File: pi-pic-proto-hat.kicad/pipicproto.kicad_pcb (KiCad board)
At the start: 2 copper layers, 65 x 56 mm, 24 parts, among them J1 RUN/~PGM~, J10 Conn_01x13_Male, J22 Conn_01x13_Male, J6 Barrel_Jack_Switch, J7 Conn_01x24_Male, J8 Conn_01x06_Male, J9 Conn_01x02_Male, P1 Conn_02x20_Odd_Even, Q1 IRF4905, U1 PIC12F675-IP

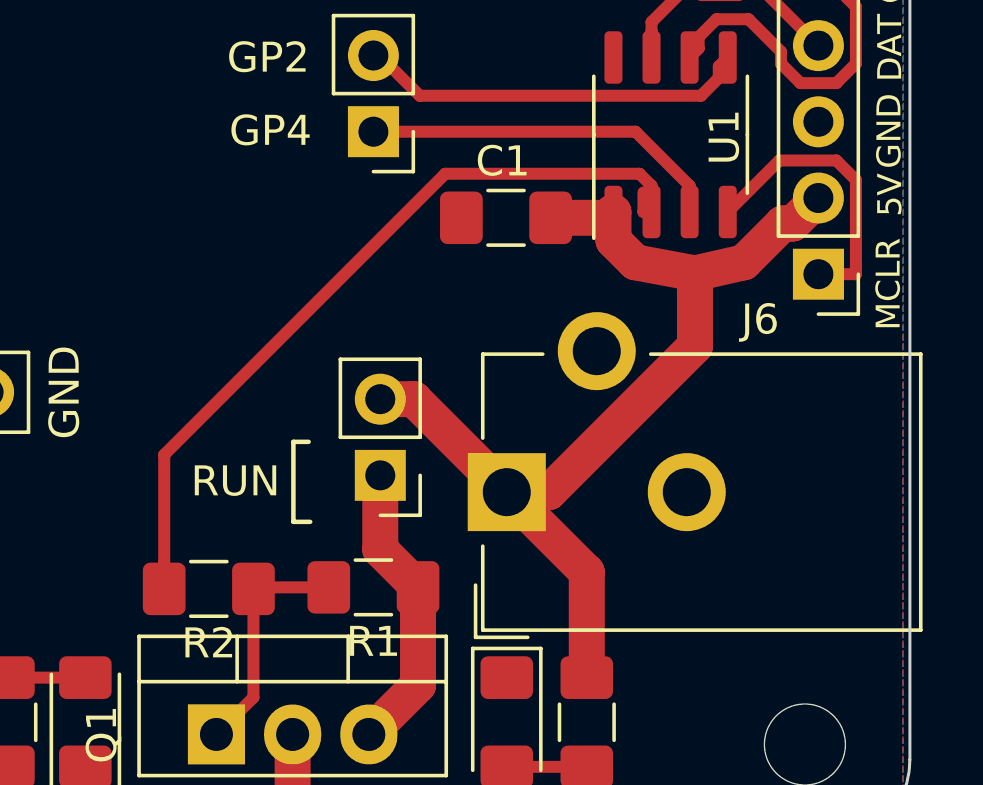
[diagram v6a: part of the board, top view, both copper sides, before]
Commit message: V2.12: changed position of RUN-jumper
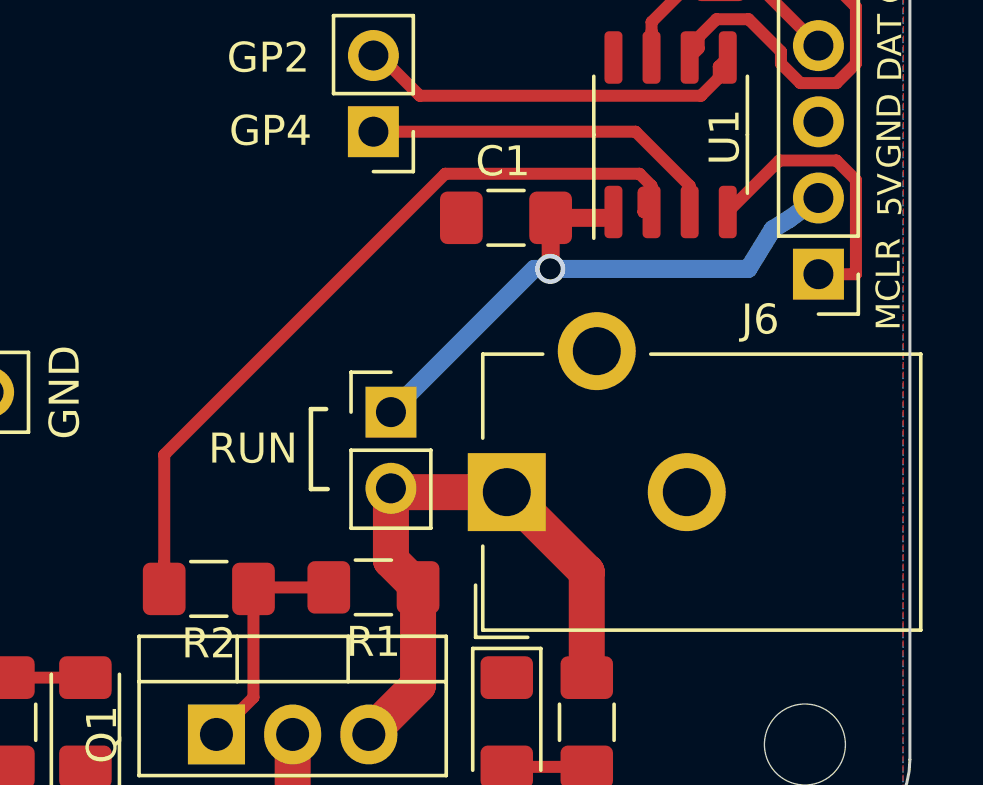
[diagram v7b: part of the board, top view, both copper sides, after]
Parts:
- moved J1 2.14 mm to (247.7, 135.4), turned to 0 degrees
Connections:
- J1 pad 1: +5P -> +5VP
- J1 pad 2: +5VP -> +5P
- J6 pad 1: +5VP -> +5P
- R4 pad 2: +5VP -> +5P
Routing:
- net +5VP: track 34.7 -> 20.9 mm, vias 0 -> 1
- net +5P: track 9.84 -> 20.5 mm
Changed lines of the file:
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@@
     (thickness 1.6)
     (drawings 67)
-    (tracks 227)
+    (tracks 225)
     (zones 0)
     (modules 24)
@@
     (fp_line (start -1.6 0.8) (end -1.6 -0.8) (layer F.Fab) (width 0.1))
     (pad 2 smd roundrect (at 1.4875 0 90) (size 1.425 1.75) (layers F.Cu F.Paste F.Mask) (roundrect_rratio 0.175439)
-      (net 30 +5VP))
+      (net 43 +5P))
     (pad 1 smd roundrect (at -1.4875 0 90) (size 1.425 1.75) (layers F.Cu F.Paste F.Mask) (roundrect_rratio 0.175439)
       (net 45 "Net-(D2-Pad2)"))
@@
   )
   (module Connector_PinHeader_2.54mm:PinHeader_1x02_P2.54mm_Vertical (layer F.Cu)
-    (at 247.3456 137.5286 180)
+    (at 247.7012 135.4204)
     (descr "Through hole straight pin header, 1x02, 2.54mm pitch, single row")
     (tags "Through hole pin header THT 1x02 2.54mm single row")
@@
       (effects (font (size 1 1) (thickness 0.15)))
     )
-    (pad 1 thru_hole rect (at 0 0 180) (size 1.7 1.7) (drill 1) (layers *.Cu *.Mask)
+    (pad 1 thru_hole rect (at 0 0) (size 1.7 1.7) (drill 1) (layers *.Cu *.Mask)
+      (net 30 +5VP))
+    (pad 2 thru_hole oval (at 0 2.54) (size 1.7 1.7) (drill 1) (layers *.Cu *.Mask)
       (net 43 +5P))
-    (pad 2 thru_hole oval (at 0 2.54 180) (size 1.7 1.7) (drill 1) (layers *.Cu *.Mask)
-      (net 30 +5VP))
     (model ${KISYS3DMOD}/Connector_PinHeader_2.54mm.3dshapes/PinHeader_1x02_P2.54mm_Vertical.wrl
       (at (xyz 0 0 0))
@@
     (fp_line (start -4.5 10.2) (end 4.5 10.2) (layer F.Fab) (width 0.1))
     (pad 1 thru_hole rect (at 0 0 90) (size 2.6 2.6) (drill 1.6) (layers *.Cu *.Mask)
-      (net 30 +5VP))
+      (net 43 +5P))
     (pad 2 thru_hole circle (at 0 6 90) (size 2.6 2.6) (drill 1.6) (layers *.Cu *.Mask)
       (net 3 GND))
@@
     (effects (font (size 0.8 0.8) (thickness 0.1)))
   )
-  (gr_line (start 244.45 139.078) (end 245.0088 139.078) (layer F.SilkS) (width 0.15))
-  (gr_line (start 244.45 136.411) (end 244.45 139.078) (layer F.SilkS) (width 0.15))
-  (gr_line (start 244.958 136.411) (end 244.45 136.411) (layer F.SilkS) (width 0.15))
-  (gr_text RUN (at 242.5196 137.7318) (layer F.SilkS)
+  (gr_line (start 245.0342 137.9858) (end 245.593 137.9858) (layer F.SilkS) (width 0.15))
+  (gr_line (start 245.0342 135.3188) (end 245.0342 137.9858) (layer F.SilkS) (width 0.15))
+  (gr_line (start 245.5422 135.3188) (end 245.0342 135.3188) (layer F.SilkS) (width 0.15))
+  (gr_text RUN (at 243.1038 136.6396) (layer F.SilkS)
     (effects (font (size 1 1) (thickness 0.15)))
   )
@@
   (segment (start 250.260001 97.480001) (end 249.01 96.23) (width 0.4) (layer F.Cu) (net 3) (status 20))
   (segment (start 255.340001 97.480001) (end 250.260001 97.480001) (width 0.4) (layer F.Cu) (net 3))
+  (segment (start 250.0491 128.9434) (end 250.0491 129.0593) (width 0.4) (layer F.Cu) (net 3))
   (segment (start 246.99 101.83) (end 246.99 103.01) (width 0.4) (layer F.Cu) (net 6) (status 20))
   (segment (start 243.93 98.77) (end 246.99 101.83) (width 0.4) (layer F.Cu) (net 6) (status 10))
@@
   (segment (start 257.479999 97.079999) (end 257.50208 97.079999) (width 0.4) (layer B.Cu) (net 29))
   (segment (start 256.63 96.23) (end 257.479999 97.079999) (width 0.4) (layer B.Cu) (net 29) (status 10))
-  (segment (start 255.118 129.698318) (end 255.118 128.7498) (width 1.2) (layer F.Cu) (net 30) (status 20))
-  (segment (start 255.844492 130.42481) (end 255.118 129.698318) (width 1.2) (layer F.Cu) (net 30))
-  (segment (start 260.763319 129.132999) (end 259.471508 130.42481) (width 1.2) (layer F.Cu) (net 30))
-  (segment (start 261.100601 129.132999) (end 260.763319 129.132999) (width 1.2) (layer F.Cu) (net 30))
-  (segment (start 261.9506 128.283) (end 261.100601 129.132999) (width 1.2) (layer F.Cu) (net 30) (status 10))
-  (segment (start 254.9101 128.9577) (end 255.118 128.7498) (width 1.2) (layer F.Cu) (net 30) (status 30))
-  (segment (start 254.8958 128.9434) (end 254.9101 128.9577) (width 1.2) (layer F.Cu) (net 30) (status 30))
-  (segment (start 253.0241 128.9434) (end 254.8958 128.9434) (width 1.2) (layer F.Cu) (net 30) (status 30))
-  (segment (start 252.970002 138.0874) (end 257.8358 133.221602) (width 1.2) (layer F.Cu) (net 30))
-  (segment (start 257.8358 133.221602) (end 257.8358 130.7976) (width 1.2) (layer F.Cu) (net 30))
-  (segment (start 251.562 138.0874) (end 252.970002 138.0874) (width 1.2) (layer F.Cu) (net 30) (status 10))
-  (segment (start 259.471508 130.42481) (end 257.8358 130.7976) (width 1.2) (layer F.Cu) (net 30))
-  (segment (start 257.8358 130.7976) (end 255.844492 130.42481) (width 1.2) (layer F.Cu) (net 30))
-  (segment (start 248.4632 134.9886) (end 247.3456 134.9886) (width 1.2) (layer F.Cu) (net 30))
-  (segment (start 251.562 138.0874) (end 248.4632 134.9886) (width 1.2) (layer F.Cu) (net 30))
-  (segment (start 254.229 140.7544) (end 251.562 138.0874) (width 1.2) (layer F.Cu) (net 30))
-  (segment (start 254.229 144.2707) (end 254.229 140.7544) (width 1.2) (layer F.Cu) (net 30))
+  (via (at 253.0098 130.6452) (size 1) (drill 0.7) (layers F.Cu B.Cu) (net 30))
+  (segment (start 253.0241 128.9434) (end 253.0241 130.6309) (width 0.6) (layer F.Cu) (net 30))
+  (segment (start 253.0241 130.6309) (end 253.0098 130.6452) (width 0.6) (layer F.Cu) (net 30))
+  (segment (start 260.96 128.9942) (end 261.9506 128.283) (width 0.6) (layer B.Cu) (net 30))
+  (segment (start 260.4266 129.3244) (end 260.96 128.9942) (width 0.6) (layer B.Cu) (net 30))
+  (segment (start 253.0098 130.6452) (end 259.6138 130.6452) (width 0.6) (layer B.Cu) (net 30))
+  (segment (start 259.6138 130.6452) (end 260.4266 129.3244) (width 0.6) (layer B.Cu) (net 30))
+  (segment (start 252.4764 130.6452) (end 247.7012 135.4204) (width 0.6) (layer B.Cu) (net 30))
+  (segment (start 253.0098 130.6452) (end 252.4764 130.6452) (width 0.6) (layer B.Cu) (net 30))
+  (segment (start 253.0241 128.9434) (end 254.9244 128.9434) (width 0.6) (layer F.Cu) (net 30))
+  (segment (start 254.229 140.7544) (end 251.562 138.0874) (width 1.2) (layer F.Cu) (net 43))
+  (segment (start 254.229 144.2707) (end 254.229 140.7544) (width 1.2) (layer F.Cu) (net 43))
   (segment (start 263.5876 114.6321) (end 264.0842 115.1287) (width 0.4) (layer F.Cu) (net 33))
   (segment (start 262.7126 114.6321) (end 263.5876 114.6321) (width 0.4) (layer F.Cu) (net 33) (status 10))
@@
   (segment (start 257.658 127.8748) (end 255.8564 126.0732) (width 0.4) (layer F.Cu) (net 42) (status 10))
   (segment (start 257.658 128.7498) (end 257.658 127.8748) (width 0.4) (layer F.Cu) (net 42) (status 30))
-  (segment (start 247.3456 140.0035) (end 248.6045 141.2624) (width 1.2) (layer F.Cu) (net 43))
-  (segment (start 247.3456 137.5286) (end 247.3456 140.0035) (width 1.2) (layer F.Cu) (net 43))
   (segment (start 248.6045 144.5247) (end 246.9646 146.1646) (width 1.2) (layer F.Cu) (net 43))
   (segment (start 248.6045 141.2624) (end 248.6045 144.5247) (width 1.2) (layer F.Cu) (net 43))
+  (segment (start 247.8282 138.0874) (end 247.7012 137.9604) (width 1.2) (layer F.Cu) (net 43))
+  (segment (start 251.562 138.0874) (end 247.8282 138.0874) (width 1.2) (layer F.Cu) (net 43))
+  (segment (start 247.7012 140.3591) (end 248.6045 141.2624) (width 1.2) (layer F.Cu) (net 43))
+  (segment (start 247.7012 137.9604) (end 247.7012 140.3591) (width 1.2) (layer F.Cu) (net 43))
   (segment (start 237.5158 144.2707) (end 234.9504 144.2707) (width 0.4) (layer F.Cu) (net 44))
   (segment (start 254.229 147.2457) (end 251.562 147.2457) (width 0.4) (layer F.Cu) (net 45))

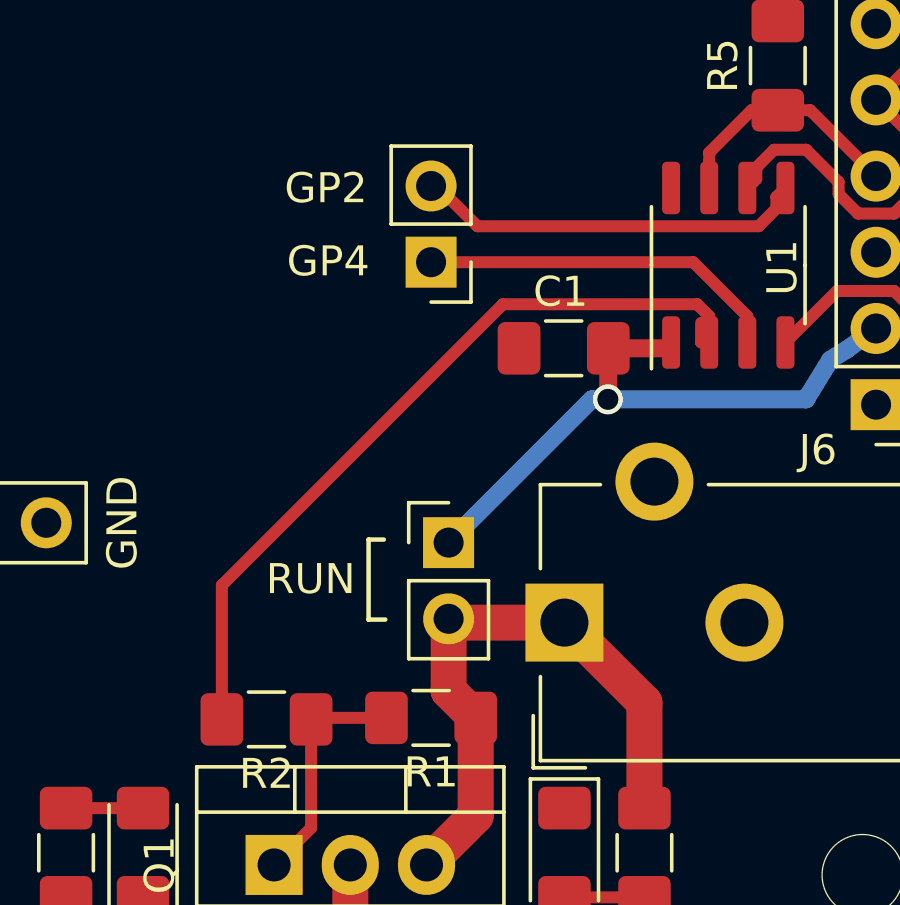
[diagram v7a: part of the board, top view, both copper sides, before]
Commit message: V2.13: added button connected to GP2
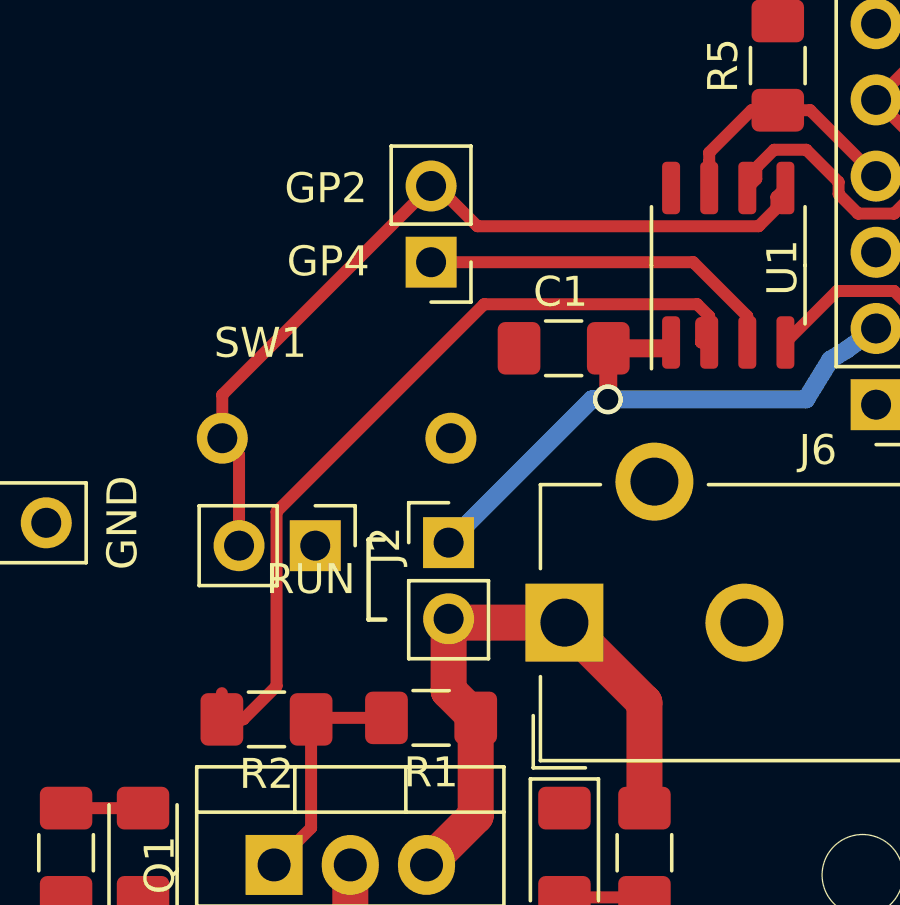
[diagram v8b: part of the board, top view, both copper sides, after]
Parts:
- added J2: Conn_SW1, Connector_PinHeader_2.54mm:PinHeader_1x02_P2.54mm_Vertical, F.Cu at (243.3, 135.5)
- added SW1: SW_Push, user:SW_PUSH_SLIM_1x4, F.Cu at (240.2, 131.9)
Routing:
- net Net-(J2-Pad2): track 12.9 -> 28.0 mm
- net Net-(R2-Pad2): track 26.7 -> 28.3 mm
